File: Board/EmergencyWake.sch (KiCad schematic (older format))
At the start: 147 parts, among them J1 USB_C_Receptacle_USB2.0, J10 Conn_01x04, J2 Micro_SD_Card_Det, J3 Conn_01x03, J4 Conn_01x02, J5 Conn_01x05, J6 Conn_01x04, J7 Conn_01x02, J8 Conn_01x04, J9 Conn_01x04, Q1 AO3400A, Q2 AO3401A, Q3 AO3400A, Q4 AO3401A, Q5 AO3401A, SW1 SW_DPDT_x2, SW2 SW_Push, SW3 SW_Push, SW4 SW_Push, U1 M24C02-WMN, U10 L9110S, U11 SRV05-4, U2 AMS1117-3.3, U3 MC34063AD, U4 STM32F407VETx, U5 WM8960, U6 173950378, U7 PT6312B, U8 EL357N-G, U9 EL357N-G, Y1 32,768, Y2 8M

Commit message: [Board] New assembly information after changing audio amp
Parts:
- U5: LCSC (none) -> C18752
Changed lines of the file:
@@
 EESchema Schematic File Version 4
-LIBS:EmergencyWake-cache
 EELAYER 30 0
 EELAYER END
@@
 F 1 "WM8960" H 11250 11300 50  0000 C CNN
 F 2 "Package_DFN_QFN:QFN-32-1EP_5x5mm_P0.5mm_EP3.45x3.45mm" H 10100 14750 50  0001 C CNN
-F 3 "" H 9550 12450 50  0001 C CNN
+F 3 "https://datasheet.lcsc.com/szlcsc/Wolfson-Microelectronics-PLC-WM8960CGEFL-RV_C18752.pdf" H 9550 12450 50  0001 C CNN
+F 4 "C18752" H 10100 12800 50  0001 C CNN "LCSC"
 	1    10100 12800
 	1    0    0    -1

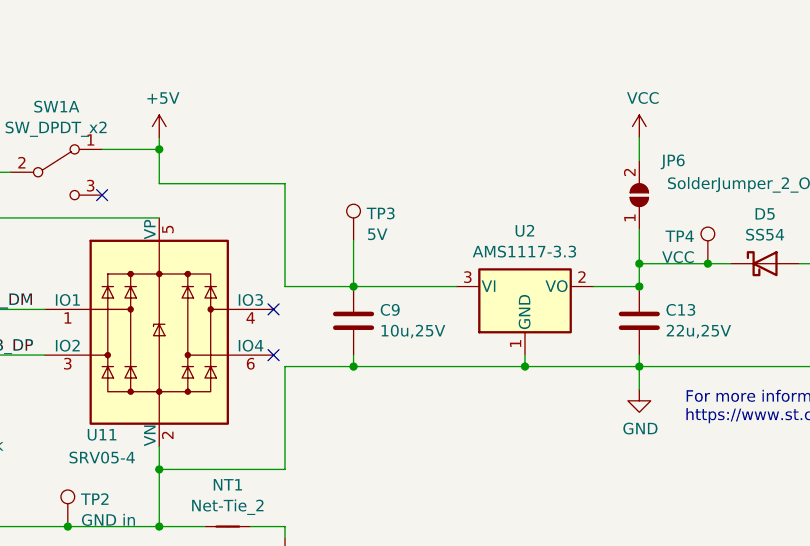
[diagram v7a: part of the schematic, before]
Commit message: [Board] Added diode in front of LDO, exported STEP filefor CAD
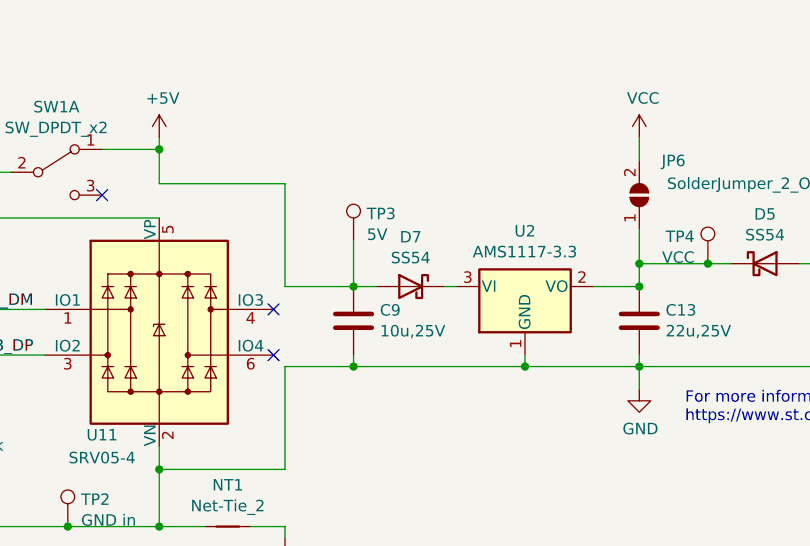
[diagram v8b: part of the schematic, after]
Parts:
- added D7: SS54, Diode_SMD:D_SMA, symbol Device:D_Schottky
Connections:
- net +5V: now also D7.2 (A); no longer U2.3 (VI)
- new net: D7.1 (K), U2.3 (VI)
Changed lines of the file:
@@
 $EndComp
 Connection ~ 4400 2000
-Wire Wire Line
-	4400 2000 4850 2000
 Text Notes 5850 2600 0    50   ~ 0
 For more information on backup battery circuit:\nhttps://www.st.com/resource/en/application_note/dm00206898.pdf
@@
 Wire Wire Line
 	9150 15100 10550 15100
+$Comp
+L Device:D_Schottky D7
+U 1 1 5EF5DA09
+P 4650 2000
+F 0 "D7" H 4650 2216 50  0000 C CNN
+F 1 "SS54" H 4650 2125 50  0000 C CNN
+F 2 "Diode_SMD:D_SMA" H 4650 2000 50  0001 C CNN
+F 3 "~" H 4650 2000 50  0001 C CNN
+F 4 "C22452" H 4650 2000 50  0001 C CNN "LCSC"
+	1    4650 2000
+	-1   0    0    -1
+$EndComp
+Wire Wire Line
+	4400 2000 4500 2000
+Wire Wire Line
+	4800 2000 4850 2000
 $EndSCHEMATC
